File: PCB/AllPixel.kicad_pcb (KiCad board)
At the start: 2 copper layers, 68.5 x 24.5 mm, 28 parts, among them CON1 ML_USB_MINI, CON2 BARREL_JACK, Q1 NPN, U1 ATMEGA16U4/32U4, Y1 16MHz

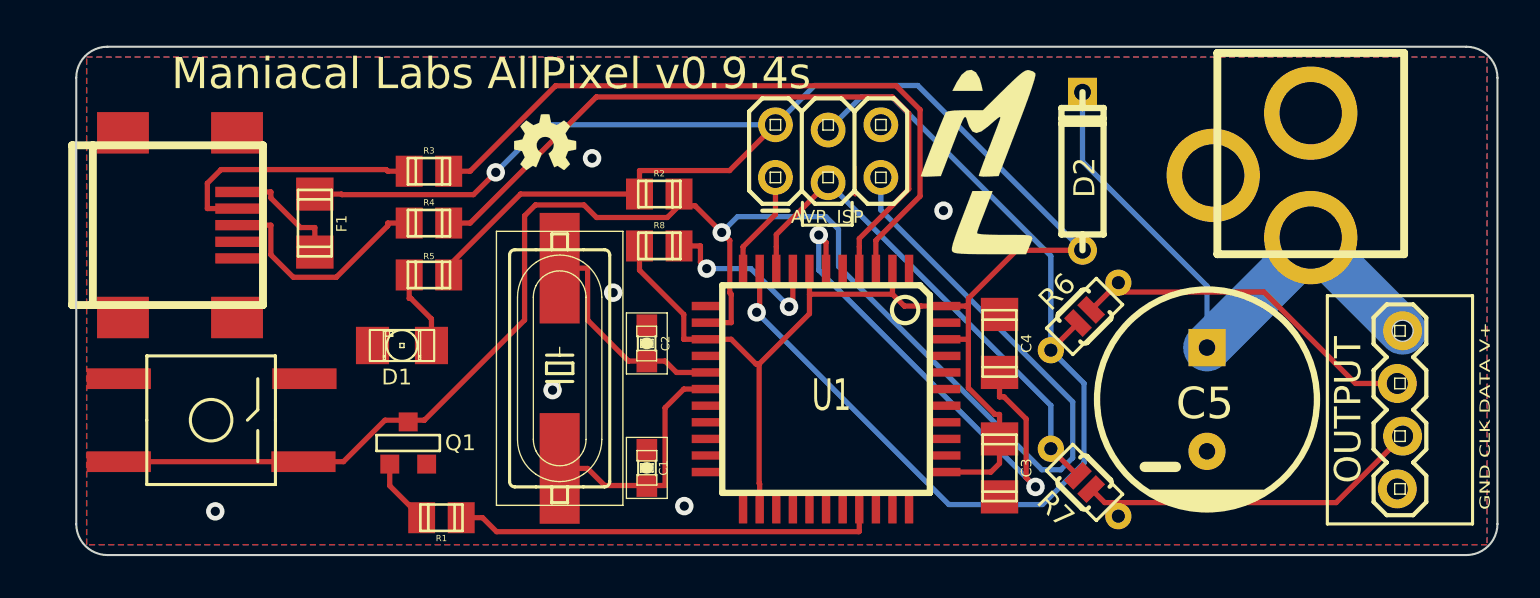
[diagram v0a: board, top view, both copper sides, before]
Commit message: updated silkscreen
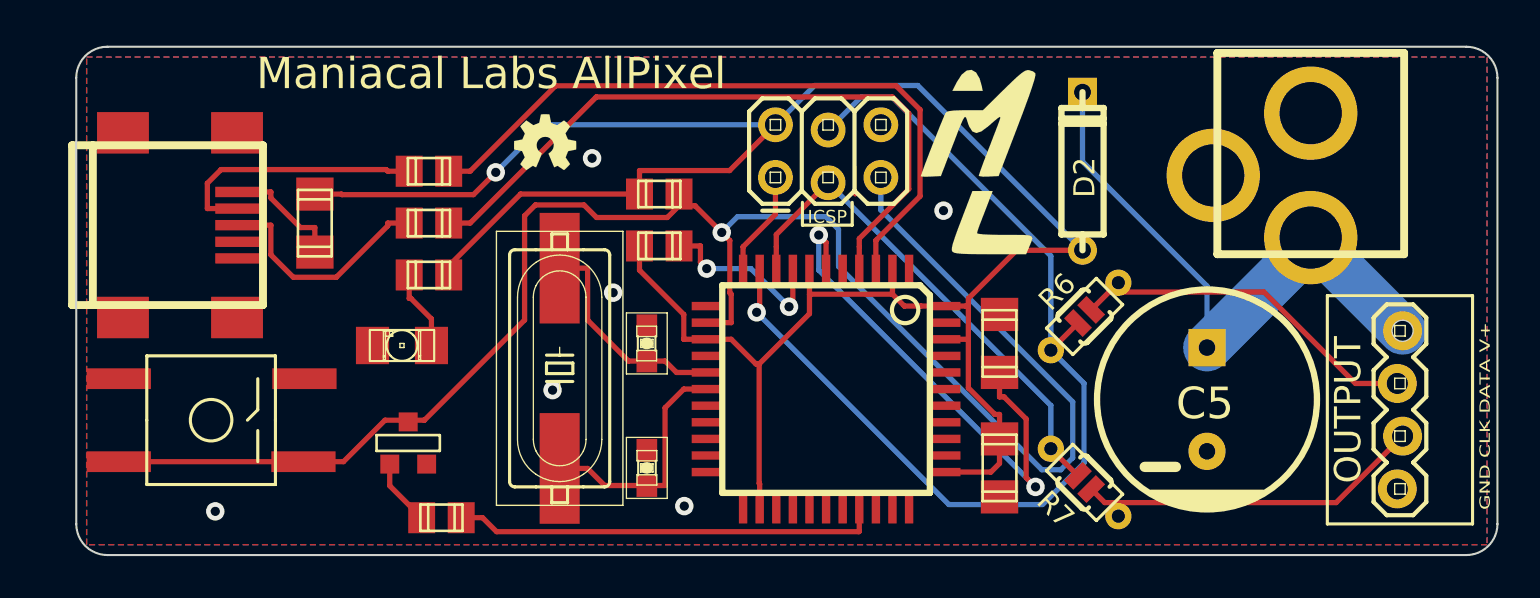
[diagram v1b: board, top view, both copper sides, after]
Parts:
- JP1: value AVR_ISP -> ICSP
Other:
- board text added: "Maniacal Labs AllPixel"
- board text removed: "Maniacal Labs AllPixel v0.9.4s"
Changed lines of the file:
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@@
-(kicad_pcb (version 3) (host pcbnew "(2013-03-04 BZR 3984)-stable")
+(kicad_pcb (version 3) (host pcbnew "(2013-07-07 BZR 4022)-stable")
   (general
     (links 65)
@@
     (pad_to_mask_clearance 0)
     (aux_axis_origin 0 0)
-    (visible_elements 7FFFFBBF)
+    (visible_elements 7FFFFB3F)
     (pcbplotparams
       (layerselection 283148289)
       (usegerberextensions true)
       (excludeedgelayer true)
-      (linewidth 0)
+      (linewidth 0.150000)
       (plotframeref false)
       (viasonmask false)
@@
       (drillshape 0)
       (scaleselection 1)
-      (outputdirectory gerberSMD/))
+      (outputdirectory gerber/))
   )
   (net 0 "")
@@
     (at 50.14 35 270)
     (attr smd)
-    (fp_text reference U1 (at 0.3 -0.26 360) (layer F.SilkS)
+    (fp_text reference U1 (at 0.3 -0.26 360) (layer F.SilkS) hide
       (effects (font (size 1.524 1.016) (thickness 0.2032)))
     )
@@
       (effects (font (size 1.27 1.27) (thickness 0.0889)))
     )
-    (fp_text value AVR_ISP (at 2.5 1.9) (layer F.SilkS)
+    (fp_text value ICSP (at 2.5 1.9) (layer F.SilkS)
       (effects (font (size 0.6238 0.6238) (thickness 0.15595)))
     )
@@
     (at 31 24.5)
     (descr "SMT capacitor, 0805")
-    (fp_text reference R3 (at 0 -0.9906) (layer F.SilkS)
+    (fp_text reference R3 (at 0 -0.9906) (layer F.SilkS) hide
       (effects (font (size 0.29972 0.29972) (thickness 0.06096)))
     )
@@
     (at 42.1 25.6)
     (descr "SMT capacitor, 0805")
-    (fp_text reference R2 (at 0 -0.9906) (layer F.SilkS)
+    (fp_text reference R2 (at 0 -0.9906) (layer F.SilkS) hide
       (effects (font (size 0.29972 0.29972) (thickness 0.06096)))
     )
@@
     (at 31.6 41.2 180)
     (descr "SMT capacitor, 0805")
-    (fp_text reference R1 (at 0 -0.9906 180) (layer F.SilkS)
+    (fp_text reference R1 (at 0 -0.9906 180) (layer F.SilkS) hide
       (effects (font (size 0.29972 0.29972) (thickness 0.06096)))
     )
@@
     (at 31 29.5)
     (descr "SMT capacitor, 0805")
-    (fp_text reference R5 (at 0 -0.9) (layer F.SilkS)
+    (fp_text reference R5 (at 0 -0.9) (layer F.SilkS) hide
       (effects (font (size 0.29972 0.29972) (thickness 0.06096)))
     )
@@
     (at 31 27)
     (descr "SMT capacitor, 0805")
-    (fp_text reference R4 (at 0 -0.9906) (layer F.SilkS)
+    (fp_text reference R4 (at 0 -0.9906) (layer F.SilkS) hide
       (effects (font (size 0.29972 0.29972) (thickness 0.06096)))
     )
@@
     (tags "LED1206 SMD")
     (attr smd)
-    (fp_text reference D1 (at 0.254 -1.524 180) (layer F.SilkS)
+    (fp_text reference D1 (at 0.254 -1.524 180) (layer F.SilkS) hide
       (effects (font (size 0.762 0.762) (thickness 0.0889)))
     )
@@
     (at 41.5 32.8 90)
     (attr smd)
-    (fp_text reference C2 (at 0 0.9 90) (layer F.SilkS)
+    (fp_text reference C2 (at 0 0.9 90) (layer F.SilkS) hide
       (effects (font (size 0.4064 0.4064) (thickness 0.0889)))
     )
@@
     (at 41.5 38.8 270)
     (attr smd)
-    (fp_text reference C1 (at 0 -0.8 270) (layer F.SilkS)
+    (fp_text reference C1 (at 0 -0.8 270) (layer F.SilkS) hide
       (effects (font (size 0.4064 0.4064) (thickness 0.0889)))
     )
@@
     (at 58.5 32.8 90)
     (descr "SMT capacitor, 1206")
-    (fp_text reference C4 (at 0 1.3 90) (layer F.SilkS)
+    (fp_text reference C4 (at 0 1.3 90) (layer F.SilkS) hide
       (effects (font (size 0.50038 0.50038) (thickness 0.11938)))
     )
@@
     (at 58.5 38.8 270)
     (descr "SMT capacitor, 1206")
-    (fp_text reference C3 (at 0 -1.3 270) (layer F.SilkS)
+    (fp_text reference C3 (at 0 -1.3 270) (layer F.SilkS) hide
       (effects (font (size 0.50038 0.50038) (thickness 0.11938)))
     )
@@
     (tags CRYSTAL)
     (attr smd)
-    (fp_text reference Y1 (at 1 0 180) (layer B.SilkS)
+    (fp_text reference Y1 (at 1 0 180) (layer B.SilkS) hide
       (effects (font (size 1.27 1.27) (thickness 0.0889)))
     )
@@
     (at 42.1 28.1)
     (descr "SMT capacitor, 0805")
-    (fp_text reference R8 (at 0 -0.9906) (layer F.SilkS)
+    (fp_text reference R8 (at 0 -0.9906) (layer F.SilkS) hide
       (effects (font (size 0.29972 0.29972) (thickness 0.06096)))
     )
@@
     (at 25.5 27 270)
     (descr "SMT capacitor, 1206")
-    (fp_text reference F1 (at 0.0254 -1.2954 270) (layer F.SilkS)
+    (fp_text reference F1 (at 0.0254 -1.2954 270) (layer F.SilkS) hide
       (effects (font (size 0.50038 0.50038) (thickness 0.11938)))
     )
@@
     (tags "CMS SOT")
     (attr smd)
-    (fp_text reference Q1 (at -2.512 0.008 180) (layer F.SilkS)
-      (effects (font (size 0.762 0.762) (thickness 0.2032)))
+    (fp_text reference Q1 (at -2.512 0.008 180) (layer F.SilkS) hide
+      (effects (font (size 0.762 0.762) (thickness 0.1905)))
     )
     (fp_text value NPN (at 0 0 180) (layer F.SilkS) hide
@@
     (effects (font (size 0.5 0.7) (thickness 0.125)))
   )
-  (gr_text "Maniacal Labs AllPixel v0.9.4s" (at 34 19.8) (layer F.SilkS)
+  (gr_text "Maniacal Labs AllPixel" (at 34 19.8) (layer F.SilkS)
     (effects (font (size 1.5 1.5) (thickness 0.3)))
   )

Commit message: Changes to AllPixel PCB for DFM.
Added USB connector with positioning holes (created new module).
Flipped fuse to simplify traces.
Enlarged holes on diode (created new module).
Replaced Ground fix trace with standard width trace (no longer have
smaller trace just for that one bodge).
Cleaned up traces in a few spots to get rid of small, oddly angled
traces.
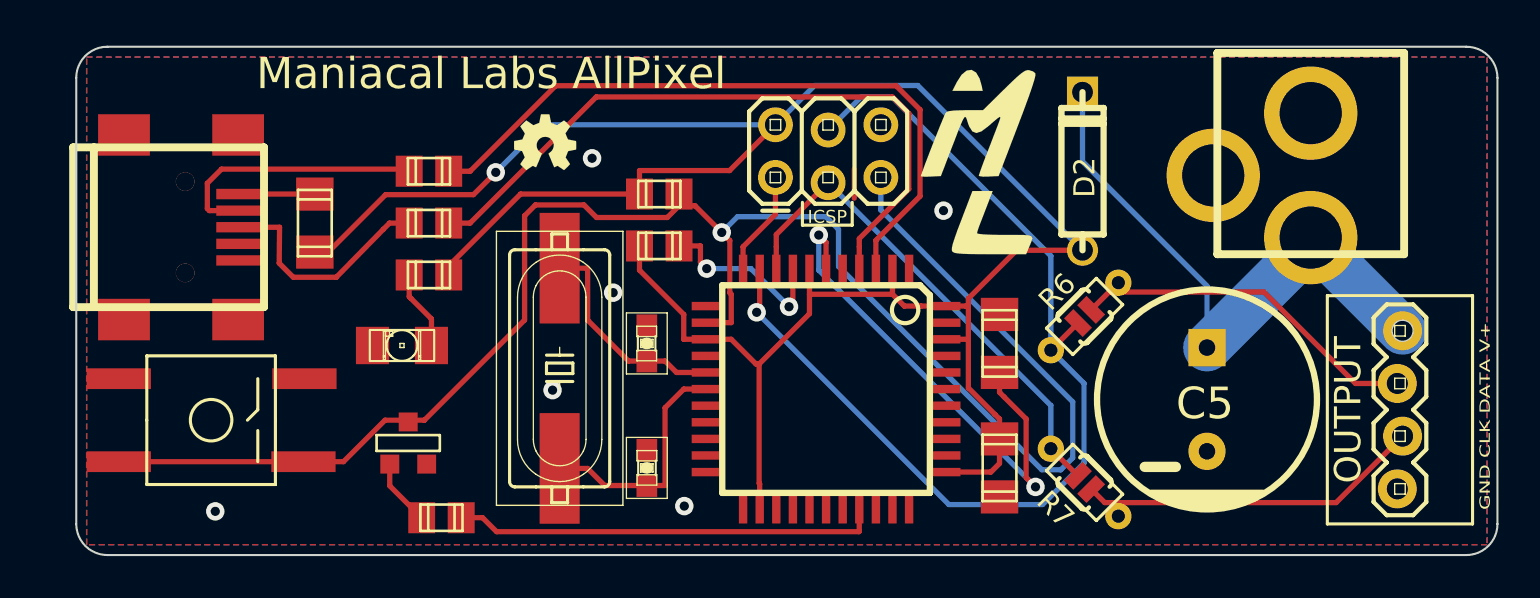
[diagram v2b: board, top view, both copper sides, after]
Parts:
- CON1: footprint ML_USB_MINI -> ML_USB_MINI_posts
- D2: footprint D3 -> ML_Diode_largerholes
- moved CON1 2.27 mm to (19.2, 25.0)
- turned F1 to 90 degrees
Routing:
- net +5V: track 5.71 -> 3.60 mm
- net VUSB: track 112.3 -> 113.3 mm
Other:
- net class groundfix removed
